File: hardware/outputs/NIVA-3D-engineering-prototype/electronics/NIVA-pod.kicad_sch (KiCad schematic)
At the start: 0 parts

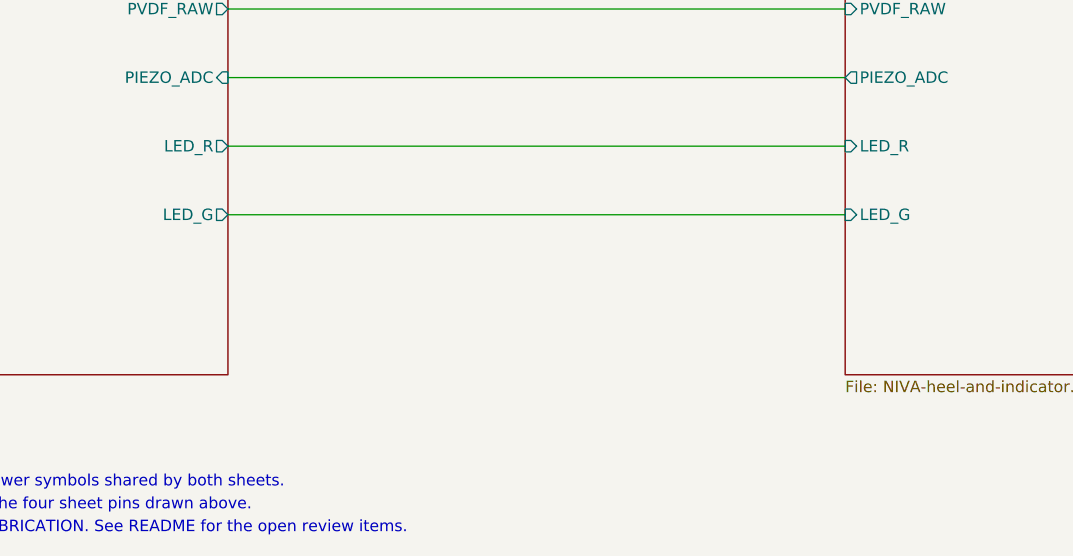
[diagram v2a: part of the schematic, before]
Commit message: Add cartridge interconnect PCB, charging dock PCB and dock enclosure; ratiometric ADC reference
- Pod schematic: MCP3208 VREF driven from VEXC (the sensor excitation rail) so every
  channel is ratiometric in hardware; CH6 reads +3V3/2 as a rail monitor.
- Cartridge: 3.4 mm interconnect strip (cell leads, polyfuse, lid-plate leads, underside
  dock pads), hand-routed; ERC/DRC clean with schematic parity.
- Dock: USB-C sink, MCP73831 charger gated by an LM393 NTC window comparator, spring
  pins to the cartridge pads; autorouted (Freerouting) and DRC clean.
- Fabrication data for both boards written only as review-only sets with open blockers.
- Dock enclosure (base, top with keyed well, tab ledge, snap latch, light pipe) generated
  from niva_layout.py; interference audit reports only the expected spring-pin contacts.
- Shared CAD helpers and cartridge builders moved to niva_cad_lib.py.

Co-Authored-By: Claude Opus 5.5 <noreply@anthropic.com>
Claude-Session: https://claude.ai/code/session_01HNzeJFE5uNHjapog53SHnm
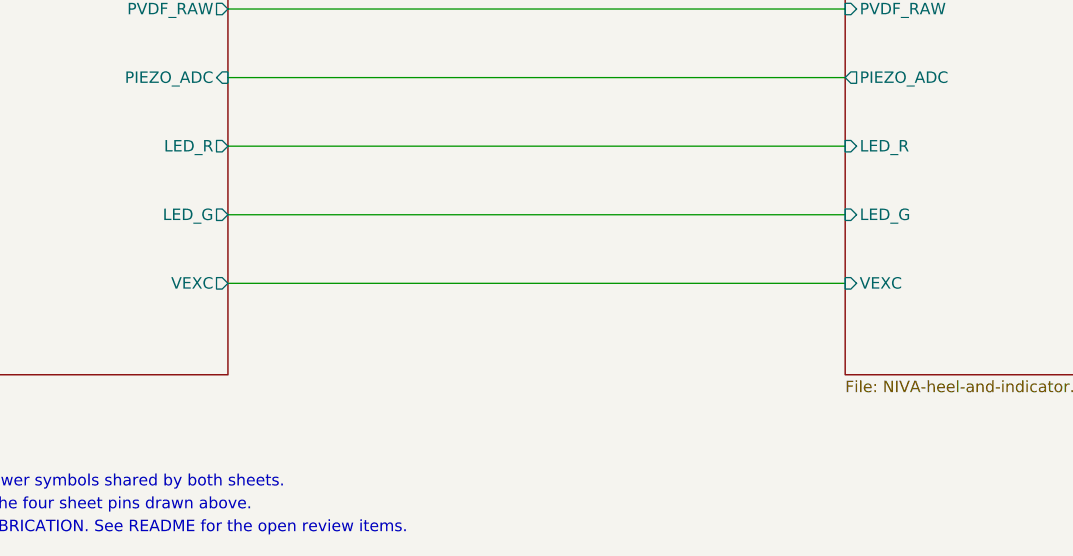
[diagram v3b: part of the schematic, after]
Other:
- sheet Controller ports: added VEXC; removed none
- sheet Heel and indicator ports: added VEXC; removed none
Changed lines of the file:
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@@
 (kicad_sch (version 20250114) (generator "eeschema") (generator_version "9.0") (paper "A4") (title_block (title "NIVA pod | Rev C hierarchy") (date "2026-09-28") (rev "C - ENGINEERING PROTOTYPE") (company "NIVA") (comment 1 "NOT FOR FABRICATION. Values, protection and layout require bench validation.") (comment 2 "Generated by work/build_niva_schematic_revC.py"))
-(sheet (at 40.64 60.96) (size 60.96 50.8) (exclude_from_sim no) (in_bom yes) (on_board yes) (dnp no) (fields_autoplaced yes) (stroke (width 0.1524) (type solid)) (fill (color 0 0 0 0.0000)) (property "Sheetname" "Controller" (at 40.64 60.26 0) (effects (font (size 1.27 1.27)) (justify left bottom))) (property "Sheetfile" "NIVA-controller.kicad_sch" (at 40.64 112.36 0) (effects (font (size 1.27 1.27)) (justify left top))) (pin "PVDF_RAW" output (at 101.6 71.12 0) (effects (font (size 1.27 1.27)) (justify right))) (pin "PIEZO_ADC" input (at 101.6 78.74 0) (effects (font (size 1.27 1.27)) (justify right))) (pin "LED_R" output (at 101.6 86.36 0) (effects (font (size 1.27 1.27)) (justify right))) (pin "LED_G" output (at 101.6 93.98 0) (effects (font (size 1.27 1.27)) (justify right))) (instances (project "NIVA-pod" (path "/39bb554a-4124-5743-9be1-ac823171f23b" (page "2")))))
-(sheet (at 170.18 60.96) (size 50.8 50.8) (exclude_from_sim no) (in_bom yes) (on_board yes) (dnp no) (fields_autoplaced yes) (stroke (width 0.1524) (type solid)) (fill (color 0 0 0 0.0000)) (property "Sheetname" "Heel and indicator" (at 170.18 60.26 0) (effects (font (size 1.27 1.27)) (justify left bottom))) (property "Sheetfile" "NIVA-heel-and-indicator.kicad_sch" (at 170.18 112.36 0) (effects (font (size 1.27 1.27)) (justify left top))) (pin "PVDF_RAW" input (at 170.18 71.12 180) (effects (font (size 1.27 1.27)) (justify left))) (pin "PIEZO_ADC" output (at 170.18 78.74 180) (effects (font (size 1.27 1.27)) (justify left))) (pin "LED_R" input (at 170.18 86.36 180) (effects (font (size 1.27 1.27)) (justify left))) (pin "LED_G" input (at 170.18 93.98 180) (effects (font (size 1.27 1.27)) (justify left))) (instances (project "NIVA-pod" (path "/39bb554a-4124-5743-9be1-ac823171f23b" (page "3")))))
+(sheet (at 40.64 60.96) (size 60.96 50.8) (exclude_from_sim no) (in_bom yes) (on_board yes) (dnp no) (fields_autoplaced yes) (stroke (width 0.1524) (type solid)) (fill (color 0 0 0 0.0000)) (property "Sheetname" "Controller" (at 40.64 60.26 0) (effects (font (size 1.27 1.27)) (justify left bottom))) (property "Sheetfile" "NIVA-controller.kicad_sch" (at 40.64 112.36 0) (effects (font (size 1.27 1.27)) (justify left top))) (pin "PVDF_RAW" output (at 101.6 71.12 0) (effects (font (size 1.27 1.27)) (justify right))) (pin "PIEZO_ADC" input (at 101.6 78.74 0) (effects (font (size 1.27 1.27)) (justify right))) (pin "LED_R" output (at 101.6 86.36 0) (effects (font (size 1.27 1.27)) (justify right))) (pin "LED_G" output (at 101.6 93.98 0) (effects (font (size 1.27 1.27)) (justify right))) (pin "VEXC" output (at 101.6 101.6 0) (effects (font (size 1.27 1.27)) (justify right))) (instances (project "NIVA-pod" (path "/d0baa98b-9520-5f20-9129-b58114850076" (page "2")))))
+(sheet (at 170.18 60.96) (size 50.8 50.8) (exclude_from_sim no) (in_bom yes) (on_board yes) (dnp no) (fields_autoplaced yes) (stroke (width 0.1524) (type solid)) (fill (color 0 0 0 0.0000)) (property "Sheetname" "Heel and indicator" (at 170.18 60.26 0) (effects (font (size 1.27 1.27)) (justify left bottom))) (property "Sheetfile" "NIVA-heel-and-indicator.kicad_sch" (at 170.18 112.36 0) (effects (font (size 1.27 1.27)) (justify left top))) (pin "PVDF_RAW" input (at 170.18 71.12 180) (effects (font (size 1.27 1.27)) (justify left))) (pin "PIEZO_ADC" output (at 170.18 78.74 180) (effects (font (size 1.27 1.27)) (justify left))) (pin "LED_R" input (at 170.18 86.36 180) (effects (font (size 1.27 1.27)) (justify left))) (pin "LED_G" input (at 170.18 93.98 180) (effects (font (size 1.27 1.27)) (justify left))) (pin "VEXC" input (at 170.18 101.6 180) (effects (font (size 1.27 1.27)) (justify left))) (instances (project "NIVA-pod" (path "/d0baa98b-9520-5f20-9129-b58114850076" (page "3")))))
 (wire (pts (xy 101.6 71.12) (xy 170.18 71.12)) (stroke (width 0) (type default)))
 (wire (pts (xy 101.6 78.74) (xy 170.18 78.74)) (stroke (width 0) (type default)))
 (wire (pts (xy 101.6 86.36) (xy 170.18 86.36)) (stroke (width 0) (type default)))
 (wire (pts (xy 101.6 93.98) (xy 170.18 93.98)) (stroke (width 0) (type default)))
+(wire (pts (xy 101.6 101.6) (xy 170.18 101.6)) (stroke (width 0) (type default)))
 (text "NIVA pod Rev C - one electrically connected hierarchy" (exclude_from_sim no) (at 40.64 30.48 0) (effects (font (size 2.5 2.5)) (justify left bottom)))
 (text "Rails +3V3, GND and VBAT are global power symbols shared by both sheets." (exclude_from_sim no) (at 40.64 124.46 0) (effects (font (size 1.27 1.27)) (justify left bottom)))
